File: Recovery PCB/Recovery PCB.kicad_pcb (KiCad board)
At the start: 4 copper layers, 82.5 x 59 mm, 95 parts, among them J1 Conn_01x02, J10 SMA_GPS, J2 Conn_01x04_Male, J3 MCU Programming Socket, J4 9V_INPUT, J5 Screw_Terminal_01x02, J6 Screw_Terminal_01x02, J7 MEM2075-00-140-01-A, J8 BLD, J9 SMA_LORA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

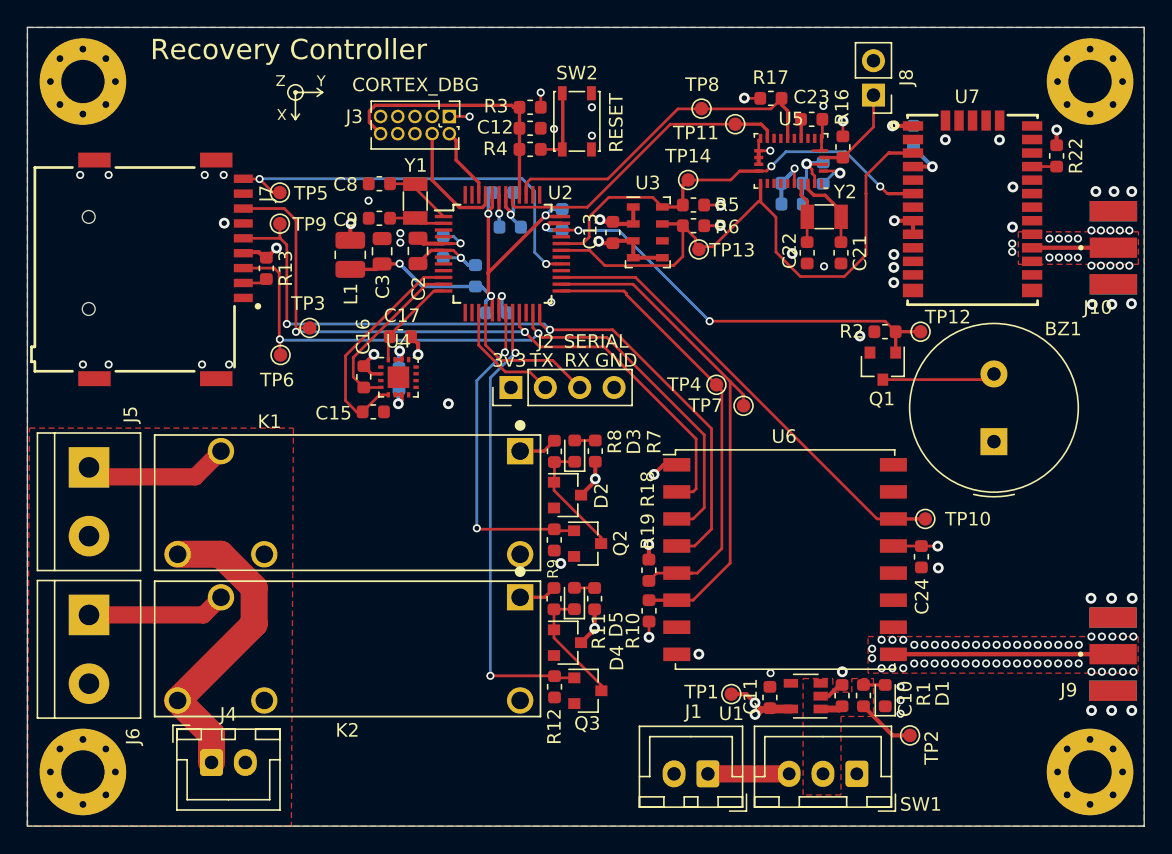
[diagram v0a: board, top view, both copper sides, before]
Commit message: Recovery PCB: Minor changes to layout.
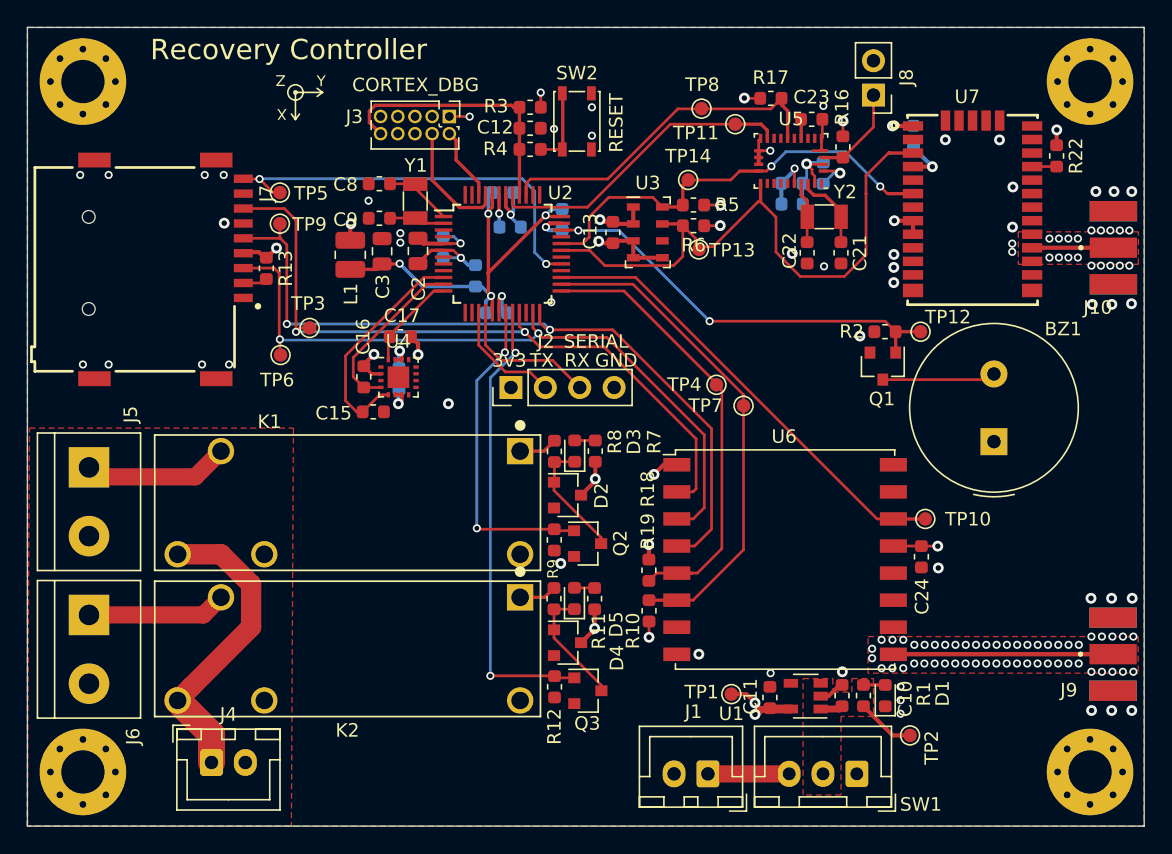
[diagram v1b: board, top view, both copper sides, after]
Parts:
- C1, C12, C4, C5, C6: value 100n -> 0.1u
- L1: value 10uH -> 10u
- R6: footprint Capacitor_SMD:C_0603_1608Metric -> Resistor_SMD:R_0603_1608Metric
- Y1: value 32.768kHz -> 32.768k
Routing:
- net /RADIO_RESET: track 38.2 -> 36.8 mm
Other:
- net class Relay Power added: clearance 0.5, trace_width 1.5, via_dia 0.6, via_drill 0.35

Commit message: Recovery: Finalize PCB.
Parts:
- added G***: LOGO, AJ_GFX:full_logo_21.3mmx9.3mm, B.Cu at (149.6, 100.0)
- added G***: LOGO, AJ_GFX:small_logo_5.71mmx5.71mm, F.Cu at (110.4, 71.9)
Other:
- board text added: "PCB-R1"
- board text added: "Recovery PCB - Rev 3.0 Part ID: PCB-R1 AstroJays Rocketry JHU, Jan 2021"

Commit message: Recovery PCB: Add active antenna supply circuit.
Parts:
- removed G***: LOGO, AJ_GFX:full_logo_21.3mmx9.3mm
- removed G***: LOGO, AJ_GFX:small_logo_5.71mmx5.71mm
- added C26: 47n, Capacitor_SMD:C_0603_1608Metric, F.Cu at (170.7, 89.0)
- added C27: 1n, Capacitor_SMD:C_0603_1608Metric, F.Cu at (169.1, 88.1)
- added L2: 47n, Inductor_SMD:L_0603_1608Metric, F.Cu at (169.1, 85.1)
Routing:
- net +3V3: track 49.9 -> 54.7 mm, vias 21 -> 22
- net /gps-module/GPS_RF: track 6.02 -> 7.54 mm
- net GND: vias 133 -> 139

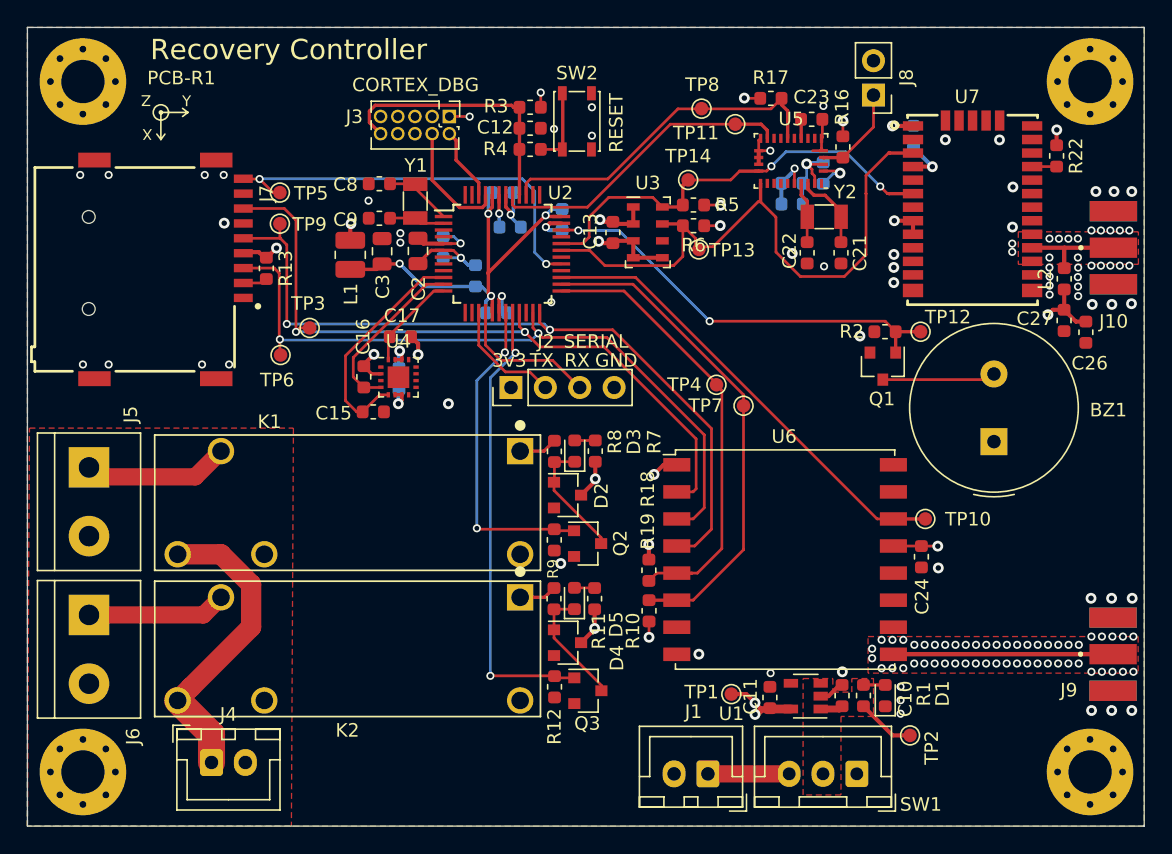
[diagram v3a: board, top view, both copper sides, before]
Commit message: Reperformed board layout with new components.
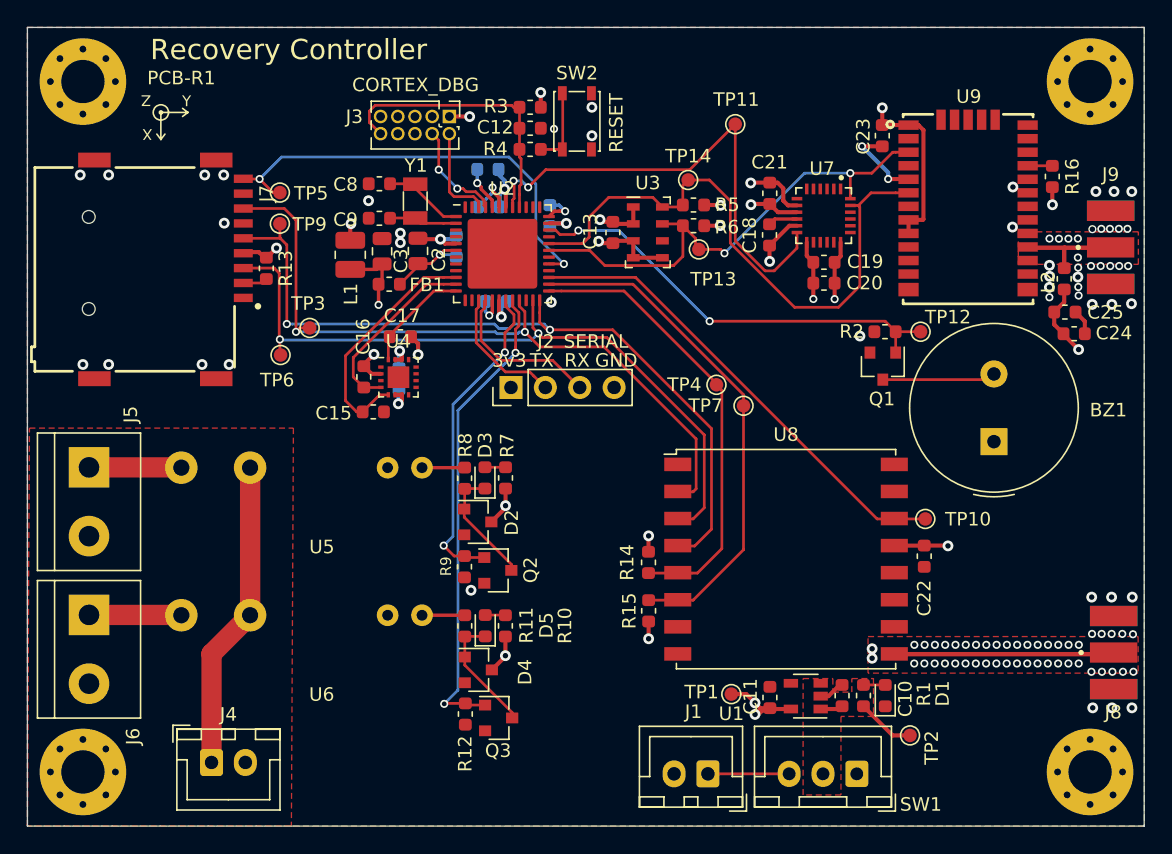
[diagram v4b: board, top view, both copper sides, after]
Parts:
- removed C26: 47n, Capacitor_SMD:C_0603_1608Metric
- removed C27: 1n, Capacitor_SMD:C_0603_1608Metric
- removed J10: SMA_GPS, Parts:RFSOLUTIONS_CON-SMA-EDGE-S
- removed K1, K2: G6RL-14-ASI-DC3, Parts:RELAY_G6RL-1
- removed R17: 4.7k, Resistor_SMD:R_0603_1608Metric
- removed R18, R19: 100k, Resistor_SMD:R_0603_1608Metric
- removed R22: 2.2k, Resistor_SMD:R_0603_1608Metric
- removed TP8: Emu-reseta, TestPoint:TestPoint_Pad_D1.0mm
- removed Y2: 32.768k, Crystal:Crystal_SMD_3215-2Pin_3.2x1.5mm
- added R14: 100k, Resistor_SMD:R_0603_1608Metric, F.Cu at (138.4, 106.0)
- added R15: 100k, Resistor_SMD:R_0603_1608Metric, F.Cu at (138.4, 109.6)
- added U8: RFM95W-915S2, RF_Module:HOPERF_RFM9XW_SMD, F.Cu at (148.5, 105.8)
- added U9: CAM-M8, Parts:CAM-M8, F.Cu at (162.0, 79.9)
- C10, C11: value 1u -> 10u
- C18: value 0.1u -> 0.47u; moved to F.Cu
- C19: value 0.12u -> 2.2u; moved to F.Cu
- C20: value 6.8n -> 0.1u; moved to F.Cu
- C21: value 22p -> 10n
- C22: value 22p -> 0.1u
- C23: value 0.1u -> 4.7u
- C24: value 0.1u -> 47n
- C25: value 4.7u -> 1n; moved to F.Cu
- FB1: moved to F.Cu
- J8: value BLD -> SMA_LORA; footprint Connector_PinHeader_2.54mm:PinHeader_1x02_P2.54mm_Vertical -> Parts:RFSOLUTIONS_CON-SMA-EDGE-S
- J9: value SMA_LORA -> SMA_GPS
- R11, R8: value 5 -> 10
- R16: value 4.7k -> 2.2k
- U1: value AP7366-33W5-7 -> XC6220B331MR
- U2: value ATSAMD21G18A-AUT -> ATSAMD21G17A-MUT; footprint Package_QFP:TQFP-48_7x7mm_P0.5mm -> Package_DFN_QFN:QFN-48-1EP_7x7mm_P0.5mm_EP5.15x5.15mm
- U5: value BNO055 -> Panasonic-PA-N; footprint Parts:LGA-28_5.2x3.8mm_P0.5mm -> Parts:Panasonic-PA-N
- U6: value RFM95W-915S2 -> Panasonic-PA-N; footprint RF_Module:HOPERF_RFM9XW_SMD -> Parts:Panasonic-PA-N
- U7: value CAM-M8 -> ICM-20689; footprint Parts:CAM-M8 -> Parts:QFN50P400X400X95-24N
- moved J8 44.8 mm to (172.7, 112.7)
- moved U5 43.5 mm to (112.8, 100.6)
- moved U6 36.2 mm to (112.8, 111.5), turned to 180 degrees
- moved J9 30.1 mm to (172.5, 82.8)
- moved C22 23.2 mm to (158.8, 105.6), turned to 270 degrees
- moved C24 20.0 mm to (169.8, 89.1), turned to 0 degrees
- moved C25 17.1 mm to (169.1, 87.5), turned to 0 degrees
- moved R16 15.6 mm to (168.2, 77.5), turned to 90 degrees
- moved U7 11.0 mm to (151.3, 80.4)
- moved D2 6.92 mm to (125.8, 103.0)
- moved D3 6.92 mm to (126.3, 99.8)
- moved R8 6.92 mm to (124.8, 99.8)
- moved Q2 6.92 mm to (127.2, 106.6)
- moved R7 6.92 mm to (127.8, 99.8)
- moved R9 6.92 mm to (124.8, 106.3)
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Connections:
- C18 pad 1: +3V3 -> Net-(C18-Pad1)
- C21 pad 1: GND -> +3V3
- C21 pad 2: Net-(C21-Pad2) -> GND
- C22 pad 1: GND -> +3V3
- C22 pad 2: Net-(C22-Pad2) -> GND
- C23 pad 1: Net-(C23-Pad1) -> +3V3
- J8 pad 1: Net-(J8-Pad1) -> /radio-915-lora/LoRa_RF
- J9 pad 1: /radio-915-lora/LoRa_RF -> /gps-module/GPS_RF
- R11 pad 1: Net-(K2-Pad1) -> Net-(R11-Pad1)
- R16 pad 2: Net-(J8-Pad1) -> /gps-module/~RST
- R8 pad 1: Net-(K1-Pad1) -> Net-(R8-Pad1)
- U2 pad 39: /IMU_RESET -> Net-(U2-Pad39)
- U5 pad 1: Net-(U5-Pad1) -> Net-(R8-Pad1)
- U5 pad 2: GND -> +3V3
- U5 pad 5: GND -> +9V
- U5 pad 6: GND -> Net-(J5-Pad1)
- U6 pad 1: GND -> Net-(R11-Pad1)
- U6 pad 2: /MISO -> +3V3
- U6 pad 5: /RADIO_CS -> +9V
- U6 pad 6: /RADIO_RESET -> Net-(J6-Pad1)
- U7 pad 1: +3V3 -> (no net)
- U7 pad 10: GND -> Net-(C18-Pad1)
- U7 pad 12: GND -> /IMU_INT
- U7 pad 13: GND -> +3V3
- U7 pad 14: GND -> (no net)
- U7 pad 15: GND -> (no net)
- U7 pad 16: Net-(U7-Pad16) -> (no net)
- U7 pad 17: /gps-module/GPS_RF -> (no net)
- U7 pad 19: GND -> (no net)
- U7 pad 2: Net-(U7-Pad2) -> (no net)
- U7 pad 20: Net-(U7-Pad20) -> (no net)
- U7 pad 21: GND -> (no net)
- U7 pad 22: GND -> Net-(U7-Pad22)
- U7 pad 23: /gps-module/~RST -> /SCL
- U7 pad 24: Net-(U7-Pad24) -> /SDA
- U7 pad 3: /SDA -> (no net)
- U7 pad 4: GND -> (no net)
- U7 pad 5: GND -> (no net)
- U7 pad 6: /SCL -> (no net)
- U7 pad 7: Net-(U7-Pad7) -> (no net)
- U7 pad 9: +3V3 -> GND
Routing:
- net /IMU_RESET: track 25.5 -> 0.00 mm
- net /IMU_INT: track 22.9 -> 36.5 mm, vias 0 -> 2
- net Net-(C3-Pad1): track 32.3 -> 45.4 mm
- net /SCL: track 32.4 -> 44.3 mm, vias 2 -> 0
- net +3V3: track 54.7 -> 63.5 mm, vias 22 -> 20
- net /SDA: track 45.3 -> 37.0 mm, vias 0 -> 2
- net Net-(J8-Pad1): track 7.01 -> 0.00 mm
- net Net-(C22-Pad2): track 5.84 -> 0.00 mm
- net Net-(C21-Pad2): track 4.53 -> 0.00 mm
- net Net-(J6-Pad1): track 10.3 -> 6.83 mm
- net Net-(J5-Pad1): track 10.3 -> 6.83 mm
- net Net-(R11-Pad1): track 0.00 -> 3.16 mm
- net Net-(R8-Pad1): track 0.00 -> 3.15 mm
- net Net-(K1-Pad1): track 2.85 -> 0.00 mm
- net Net-(K2-Pad1): track 2.78 -> 0.00 mm
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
